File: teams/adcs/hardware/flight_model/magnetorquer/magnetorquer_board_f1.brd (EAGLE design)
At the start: 90 x 90 mm, 60 parts, among them U5 LTC3624

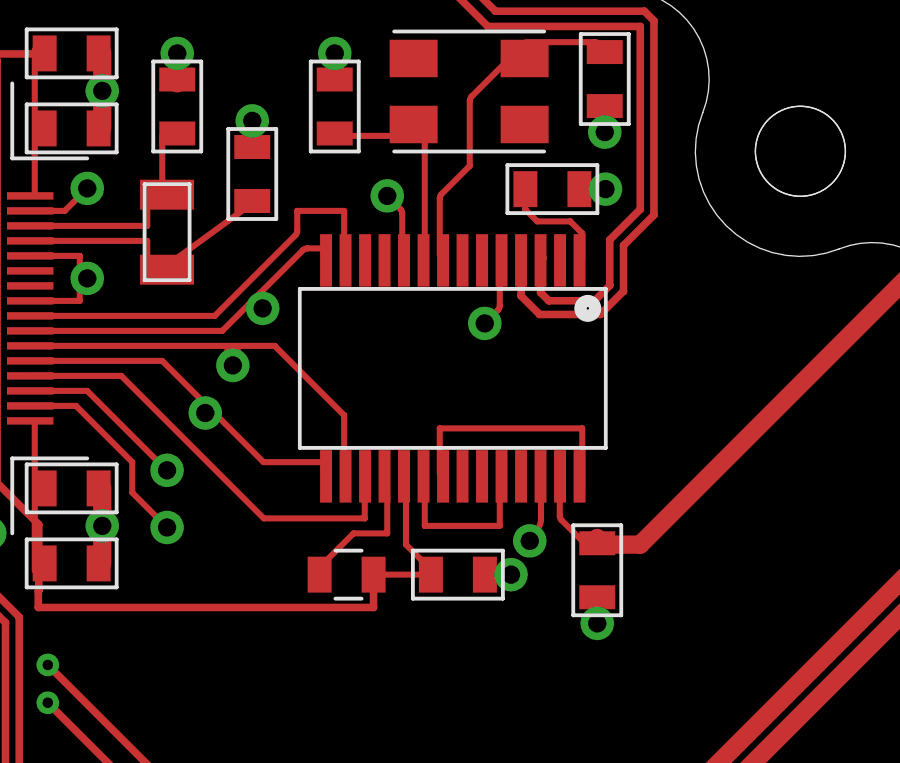
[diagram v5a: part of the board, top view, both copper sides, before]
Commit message: ADCS/MT: Reconnect leg of CAN transceiver that somehow got unrouted
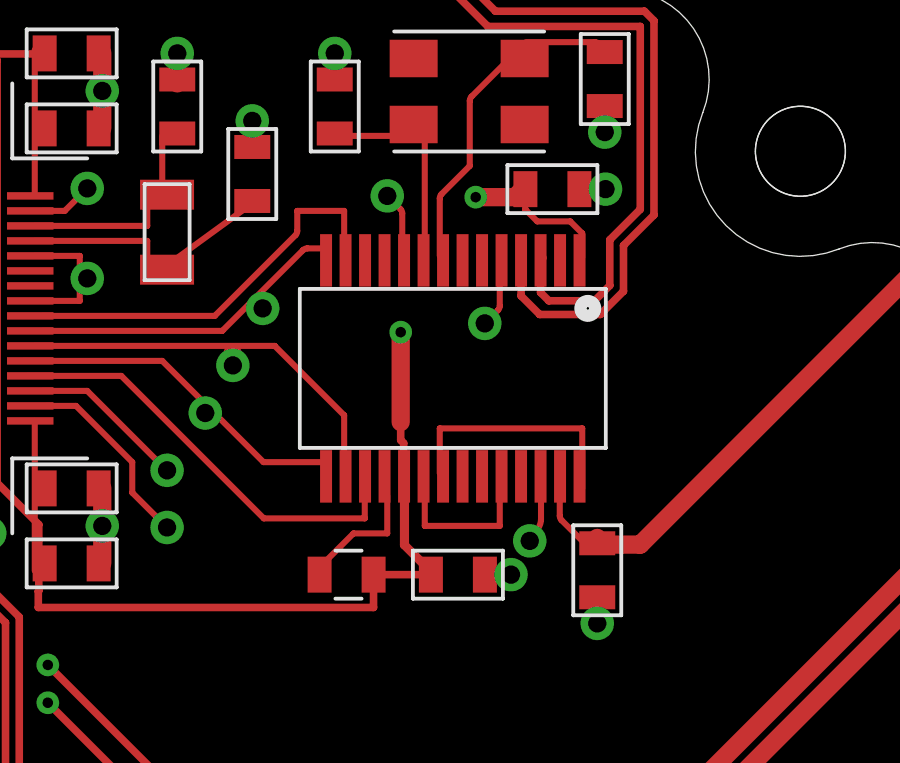
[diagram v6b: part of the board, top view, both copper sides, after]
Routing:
- net +3V3: track 88.0 -> 105.7 mm, vias 6 -> 8
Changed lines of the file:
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@@
 <wire x1="31.9275" y1="67.7525" x2="31.5195" y2="68.1605" width="0.6096" layer="1"/>
 <wire x1="31.5195" y1="68.1605" x2="31.5195" y2="68.2525" width="0.6096" layer="1"/>
-<wire x1="71.4276" y1="41.417" x2="74.5776" y2="54.267" width="0" layer="19" extent="1-1"/>
-<wire x1="69.596" y1="41.2115" x2="71.4276" y2="41.417" width="0" layer="19" extent="1-1"/>
-<wire x1="19.304" y1="73.406" x2="18.796" y2="73.406" width="0" layer="19" extent="1-2"/>
+<wire x1="74.5776" y1="54.267" x2="74.3106" y2="54" width="0.6096" layer="1"/>
+<wire x1="74.3106" y1="54" x2="73" y2="54" width="0.6096" layer="1"/>
+<via x="73" y="54" extent="1-16" drill="0.35"/>
+<wire x1="73" y1="54" x2="70.5" y2="51.5" width="0.6096" layer="2"/>
+<wire x1="70.5" y1="51.5" x2="70.5" y2="49.5" width="0.6096" layer="2"/>
+<via x="70.5" y="49.5" extent="1-16" drill="0.35"/>
+<wire x1="70.5" y1="49.5" x2="70.5" y2="46.5" width="0.6096" layer="1"/>
+<wire x1="70.5" y1="46.5" x2="70.5" y2="45.9" width="0.254" layer="1"/>
+<wire x1="70.5" y1="45.9" x2="70.6" y2="45.8" width="0.254" layer="1"/>
+<wire x1="70.6" y1="45.8" x2="70.6" y2="42.4" width="0.254" layer="1"/>
+<wire x1="71.4276" y1="41.5724" x2="71.4276" y2="41.417" width="0.254" layer="1"/>
+<wire x1="70.6" y1="42.4" x2="71.4276" y2="41.5724" width="0.254" layer="1"/>
+<wire x1="71.4276" y1="41.417" x2="69.6745" y2="41.417" width="0.254" layer="1"/>
+<wire x1="69.6745" y1="41.417" x2="69.5325" y2="41.275" width="0.254" layer="1"/>
 <wire x1="19.812" y1="73.406" x2="19.304" y2="73.406" width="0" layer="19" extent="1-1"/>
+<wire x1="18.796" y1="73.406" x2="19.304" y2="73.406" width="0" layer="19" extent="1-2"/>
 </signal>
 <signal name="+5V">
